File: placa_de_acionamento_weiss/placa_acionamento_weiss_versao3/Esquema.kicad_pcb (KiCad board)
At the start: 2 copper layers, 69.8 x 58.5 mm, 29 parts, among them Q1 IRF540, Q2 IRF540, Q3 IRF540

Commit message: Modelo 3D da placa de processamento (.f3d e .step)
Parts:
- SP0: footprint AL11P -> buzzer:AL11P
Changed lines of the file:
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@@
 		)
 		(embedded_fonts no)
+		(model "${MODELOS_3D_CRD}/Mosfet IRF540.step"
+			(offset
+				(xyz 0 -5.5 12.5)
+			)
+			(scale
+				(xyz 1 1 1)
+			)
+			(rotate
+				(xyz -90 -0 90)
+			)
+		)
 	)
 	(footprint "dummyfp3"
@@
 		(embedded_fonts no)
 	)
-	(footprint "AL11P"
+	(footprint "buzzer:AL11P"
 		(layer "F.Cu")
 		(at 144.5741 85.8521 90)
@@
 			(layer "F.SilkS")
 		)
-		(pad "+" thru_hole oval
-			(at 2.54 0 180)
-			(size 2.794 1.397)
+		(pad "+" thru_hole roundrect
+			(at 2.286 0 90)
+			(size 1.905 1.905)
 			(drill 1.016)
 			(layers "*.Cu" "*.Mask")
 			(remove_unused_layers no)
+			(roundrect_rratio 0.25)
+			(chamfer_ratio 0.2928932188)
+			(chamfer top_left top_right bottom_left bottom_right)
 			(net "VCC")
 			(solder_mask_margin 0.1016)
 			(thermal_bridge_angle 0)
 		)
-		(pad "-" thru_hole oval
-			(at -2.54 0 180)
-			(size 2.794 1.397)
+		(pad "-" thru_hole roundrect
+			(at -2.286 0 90)
+			(size 1.905 1.905)
 			(drill 1.016)
 			(layers "*.Cu" "*.Mask")
 			(remove_unused_layers no)
+			(roundrect_rratio 0.25)
+			(chamfer_ratio 0.2928932188)
+			(chamfer top_left top_right bottom_left bottom_right)
 			(net "N$2")
 			(solder_mask_margin 0.1016)

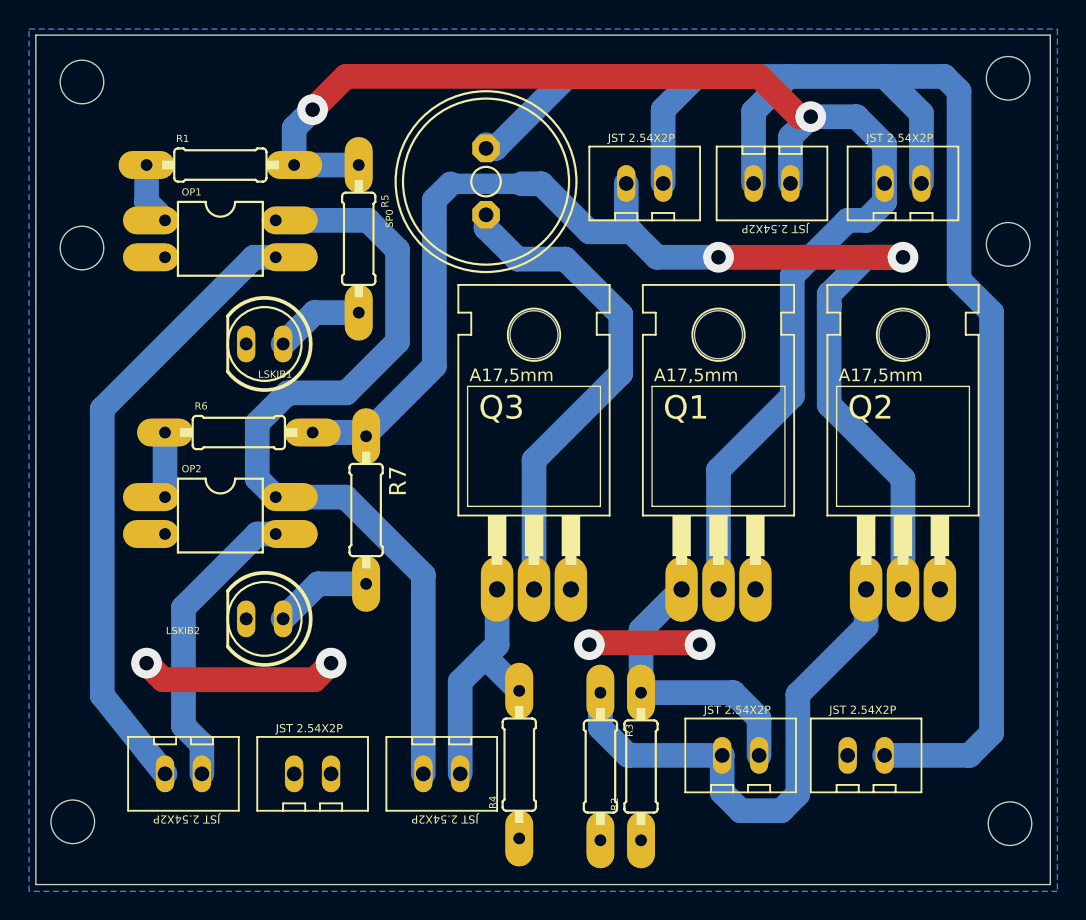
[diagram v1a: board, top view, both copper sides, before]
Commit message: Modelo 3D da placa de processamento
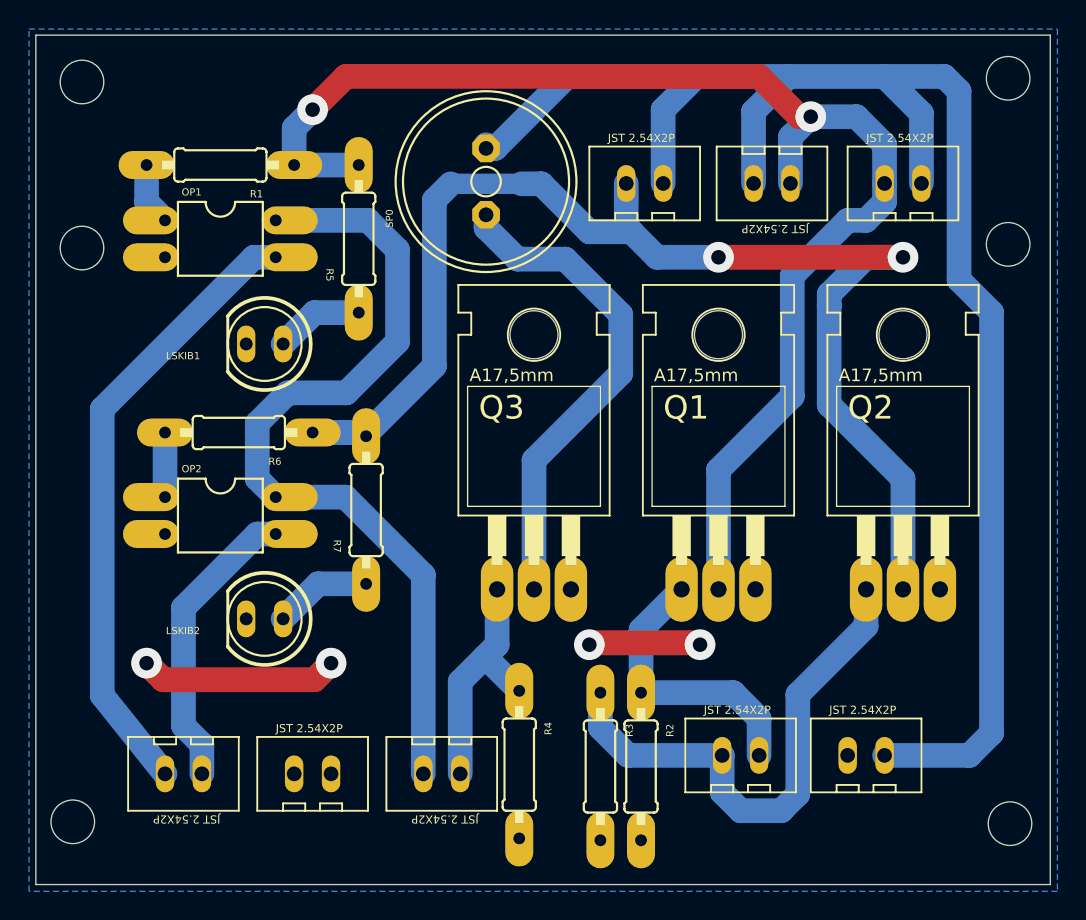
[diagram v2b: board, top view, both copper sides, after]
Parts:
- BATERIA0, GND0, S1-S2, SK1-SK2, SKIB1.0, SKIB1.1, SKIB2, UNK3.3-BUZ0: footprint JST2.54X2P_FOOTPRINT_39051337 -> CompAcionamento:JST2.54X2P_FOOTPRINT_39051337
- LSKIB1, LSKIB2: footprint LED5MM -> CompAcionamento:LED_5MM
- OP1, OP2: footprint DIL04_320 -> CompAcionamento:PC817
- Q1, Q2, Q3: footprint TO220_396 -> CompAcionamento:IRF540
- R1, R2, R3, R4, R5, R6, R7: footprint 0207_10 -> CompAcionamento:Resistor
- SP0: value AL11P -> BUZZER; footprint buzzer:AL11P -> CompAcionamento:BUZZER
